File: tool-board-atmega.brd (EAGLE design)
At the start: 144 x 104 mm, 86 parts, among them IC3 ATMEGA2560-16AU, IC4 ATMEGA8U2-MU, Q1 16MHz, X1 22-23-2041, X2 MICROUSB_VERTICAL, X3 22-23-2041, X4 22-23-2041, Y2 16MHz

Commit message: significant routing done, need to beef up stepper related lines, add 24V stepper
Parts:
- moved U$2 191.4 mm to (-36.3, 44.8)
- moved U$3 191.4 mm to (-40.1, 44.8)
- moved U$4 191.4 mm to (-44.0, 44.8)
- moved U$5 191.4 mm to (-47.8, 44.8)
- moved F2 1.25 mm to (-19.6, 37.1)
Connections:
- new net N$38: F2.2, U$9.P$1
- net VCCPIN: no longer F2.2, U$9.P$1
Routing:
- net N$16: track 0.00 -> 148.2 mm, vias 0 -> 2
- net N$15: track 0.00 -> 129.1 mm, vias 0 -> 4
- net PB5: track 0.00 -> 115.4 mm, vias 0 -> 4
- net PB6: track 0.00 -> 114.3 mm, vias 0 -> 6
- net PB7: track 0.00 -> 104.5 mm, vias 0 -> 2
- net +12V: track 0.00 -> 97.8 mm
- net RESET: track 0.00 -> 97.3 mm, vias 0 -> 4
- net PA5: track 0.00 -> 95.5 mm, vias 0 -> 2
- net PA6: track 0.00 -> 92.6 mm, vias 0 -> 2
- net PA7: track 0.00 -> 77.5 mm, vias 0 -> 2
- net +5V: track 1.09 -> 72.0 mm, vias 1 -> 20
- net D-: track 0.00 -> 70.4 mm, vias 0 -> 1
- net PE0: track 0.00 -> 59.8 mm, vias 0 -> 2
- net PE1: track 0.00 -> 57.8 mm, vias 0 -> 4
- net D+: track 0.00 -> 53.4 mm, vias 0 -> 2
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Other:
- outline, holes or cut-outs redrawn

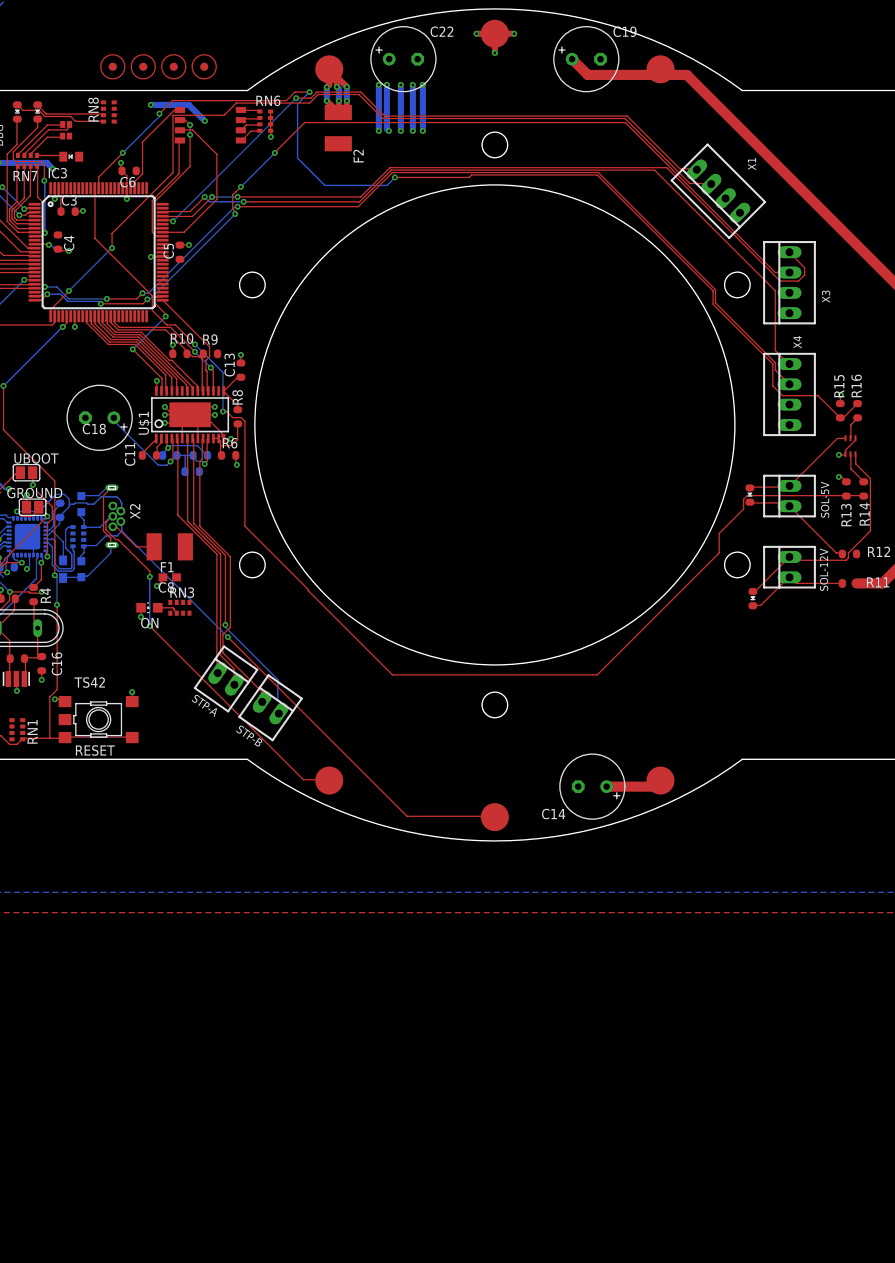
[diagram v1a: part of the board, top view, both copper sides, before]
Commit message: Beefed up 12V stepper lines, still need to work on 24V stepper lines.  Need to switch connectors for higher current ones
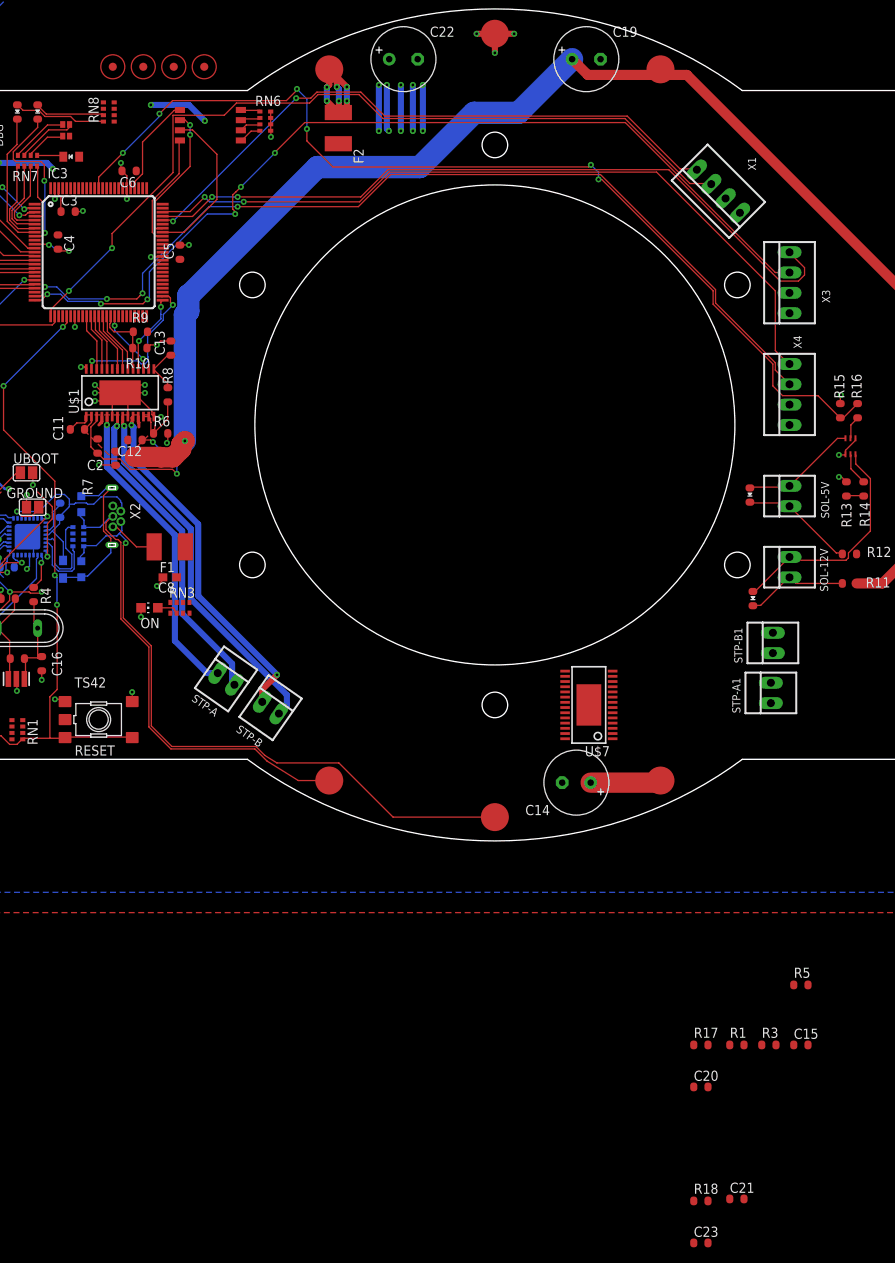
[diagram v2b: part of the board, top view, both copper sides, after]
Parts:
- removed C18: 100uF, rcl:E3,5-8
- added C15: .01u, SmartPrj:C0603-ROUND
- added C20: .47u, SmartPrj:C0603-ROUND
- added C21, C23: .1u, SmartPrj:C0603-ROUND
- added R1: 30k, SmartPrj:R0603-ROUND
- added R17, R5: 4.7k, SmartPrj:R0603-ROUND
- added R18: 1M, SmartPrj:R0603-ROUND
- added R3: 50k, SmartPrj:R0603-ROUND
- added STP-A1, STP-B1: 22-23-2021, con-molex:22-23-2021
- added U$7: DRV8825, ClinicalRobotics:DRV8825
- moved C2 9.71 mm to (-47.4, -4.15), flipped to the top, turned to 270 degrees
- moved C11 9.57 mm to (-52.2, -0.56)
- moved C13 9.17 mm to (-40.5, 9.60)
- moved R8 9.17 mm to (-40.9, 3.77)
- moved R9 9.17 mm to (-44.3, 11.6)
- moved U$1 9.17 mm to (-46.9, 4.02)
- moved R7 9.09 mm to (-49.7, -2.64), flipped to the top, turned to 90 degrees
- moved R6 8.93 mm to (-41.8, -1.06)
- moved C12 8.38 mm to (-45.0, -1.88), flipped to the top, turned to 180 degrees
- moved R10 5.06 mm to (-44.4, 9.61), turned to 0 degrees
- moved C14 2.06 mm to (10.2, -44.7)
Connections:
- removed net +12VIN: C12.2, C18.+, C2.1, R7.2, U$1.11, U$1.4
- removed net PC0: IC3.53
- removed net PC1: IC3.54
- removed net PC2: IC3.55
- removed net PC3: IC3.56
- removed net PC4: IC3.57
- removed net PC5: IC3.58
- removed net PC6: IC3.59
- removed net PC7: IC3.60
- new net DECAY-1: IC3.59, R17.1, R5.2, U$7.19
- new net DIR-1: IC3.58, U$7.20
- new net MODE0-1: IC3.55, U$7.24
- new net MODE1-1: IC3.54, U$7.25
- new net MODE2-1: IC3.53, U$7.26
- new net N$39: C15.1, U$7.1
- new net N$40: C15.2, U$7.2
- new net N$41: C20.1, R3.2, U$7.15
- new net N$42: R1.1, R3.1, U$7.12, U$7.13
- new net N$43: STP-A1.1, U$7.5
- new net N$44: STP-A1.2, U$7.7
- new net N$45: STP-B1.2, U$7.8
- new net N$46: STP-B1.1, U$7.10
- new net NENBL-1: IC3.57, U$7.21
- new net NFAULT-1: U$7.18
- new net NHOME-1: U$7.27
- new net NRESET-1: U$7.16
- new net NSLEEP-1: IC3.60, U$7.17
- new net NSTEP-1: IC3.56, U$7.22
- new net VCP-1: C21.1, R18.1, U$7.3
- net +12V: now also C12.2, C2.1, R7.2, U$1.11, U$1.4
- net +24V: now also C21.2, C23.1, R18.2, U$7.11, U$7.4
- net +5V: now also R5.1
- net GND: now also C20.2, C23.2, R1.2, R17.2, U$7.14, U$7.28, U$7.6, U$7.9, U$7.HEAT; no longer C18.-
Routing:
- net N$16: track 148.2 -> 2.19 mm, vias 2 -> 0
- net +12V: track 97.8 -> 186.8 mm, vias 0 -> 1
- net +12VIN: track 23.7 -> 0.00 mm, vias 2 -> 0
- net VCP: track 8.03 -> 23.1 mm, vias 1 -> 2
- net D-: track 70.4 -> 82.5 mm
- net NSLEEP: track 18.2 -> 8.14 mm
- net DECAY: track 19.5 -> 9.59 mm
- net DIR: track 16.2 -> 7.78 mm
- net MODE2: track 15.5 -> 7.17 mm
- net MODE0: track 15.6 -> 7.33 mm
- net MODE1: track 15.5 -> 7.29 mm
- net NENBL: track 15.9 -> 7.68 mm
- net NSTEP: track 15.9 -> 7.70 mm
- net D+: track 53.4 -> 60.6 mm, vias 2 -> 0
- net N$7: track 31.4 -> 38.6 mm, vias 0 -> 1
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- added copper zone on layer 1, net +12V

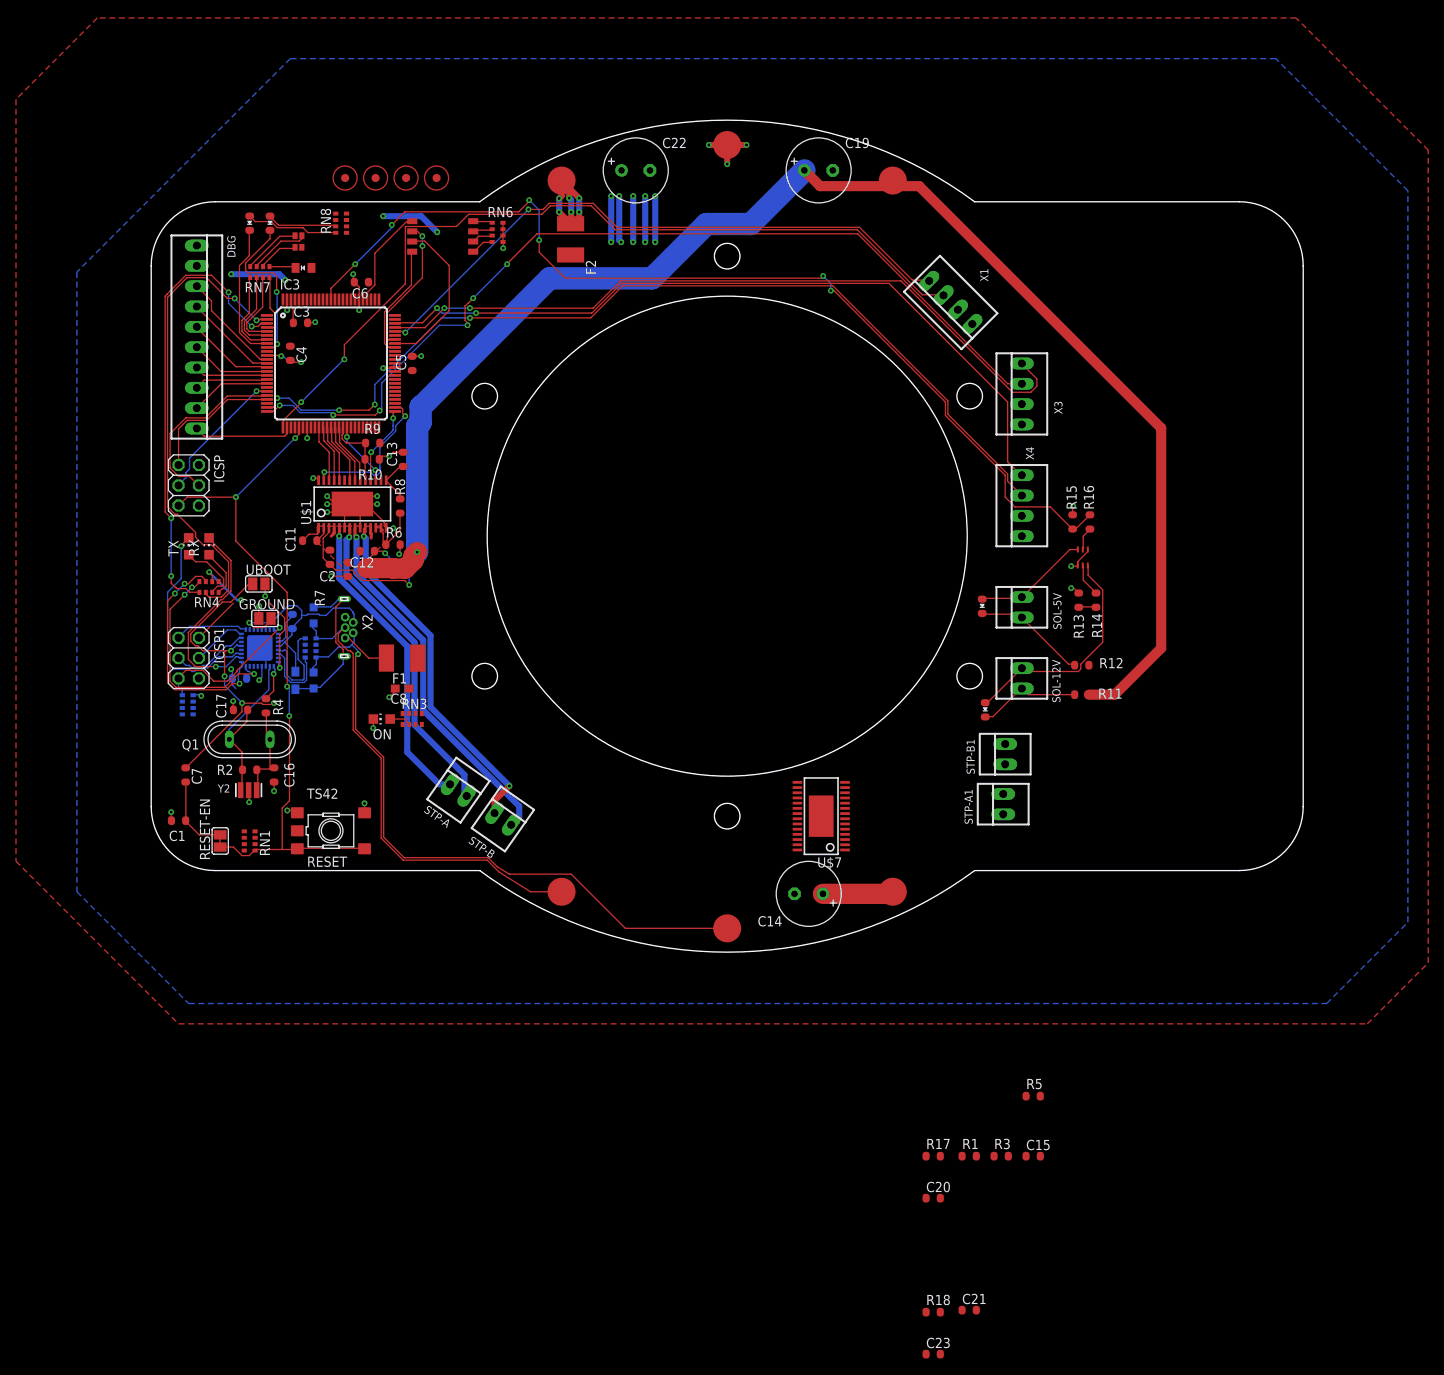
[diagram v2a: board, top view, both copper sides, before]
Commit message: Fixed stepper motor drivers for cleaner routing, moved them closer to power pogos
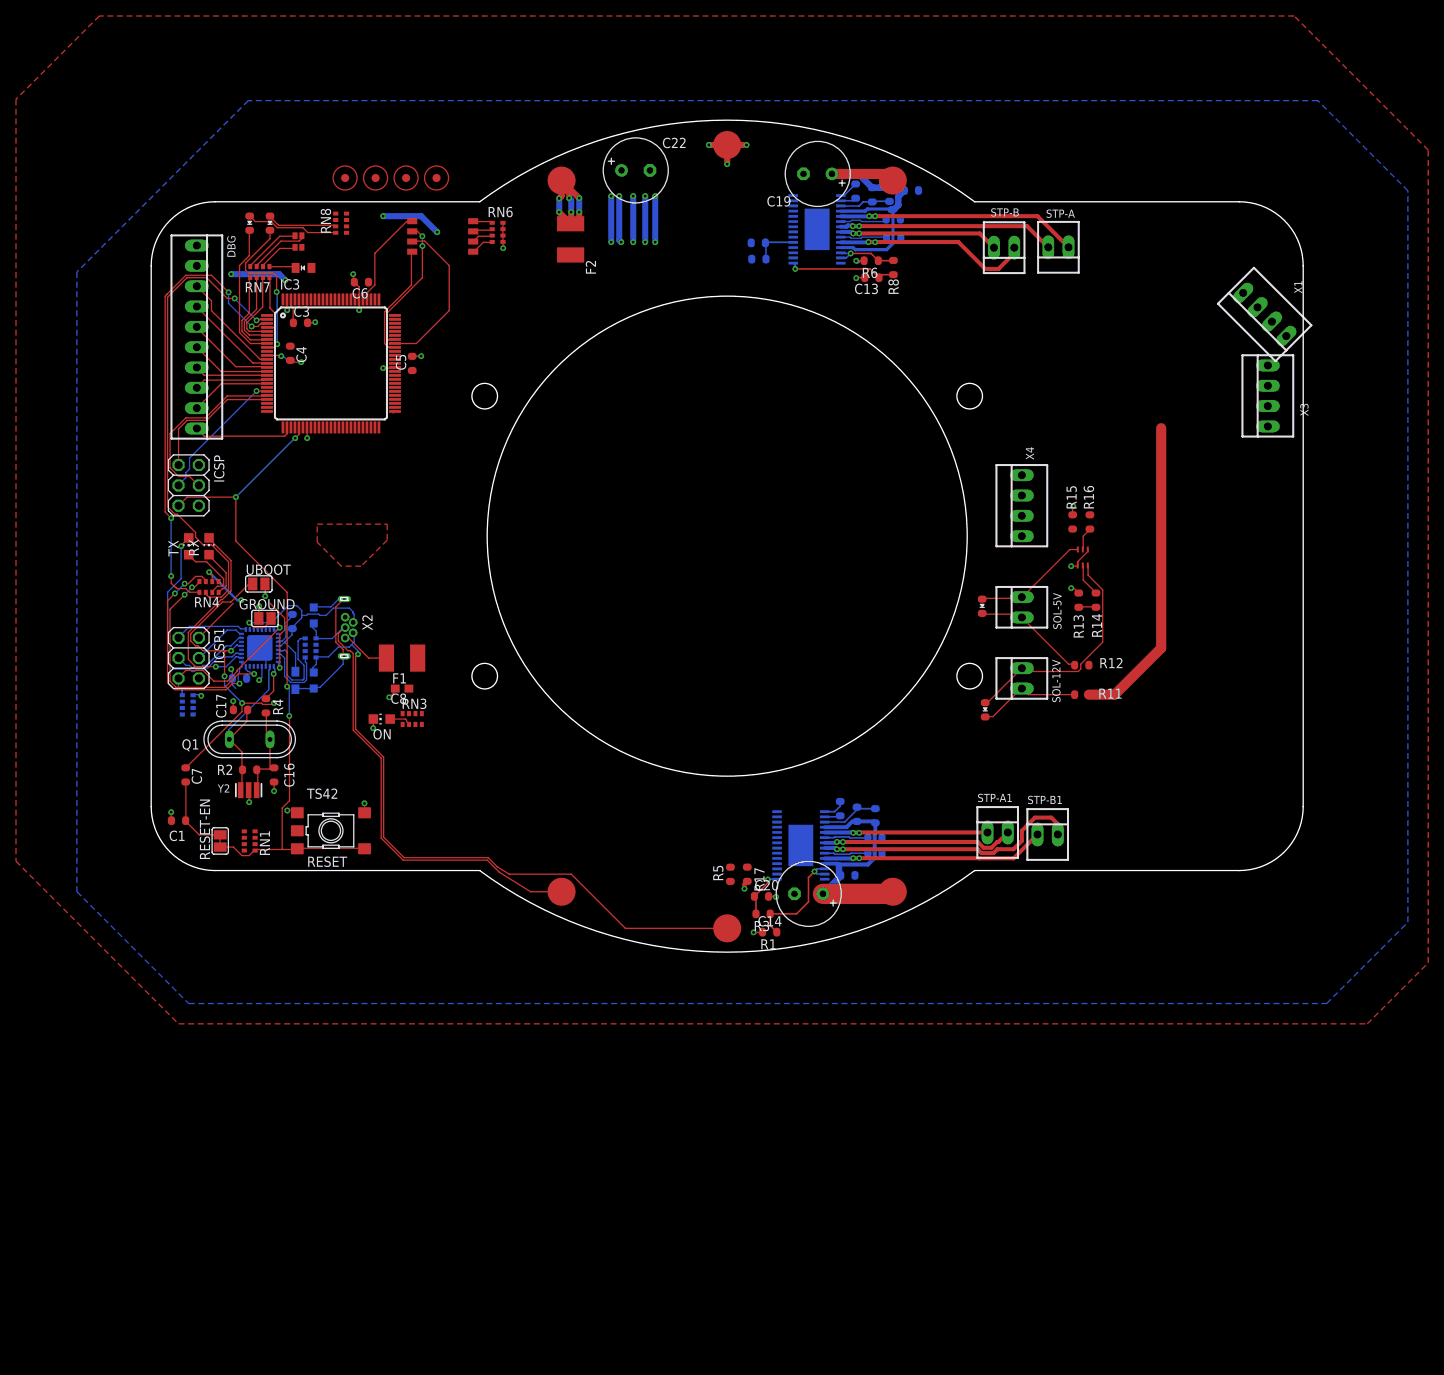
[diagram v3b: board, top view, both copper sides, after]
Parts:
- added R19, R20, R21, R22: 200m, SmartPrj:R0603-ROUND
- moved STP-A 101.1 mm to (41.4, 36.1), turned to 180 degrees
- moved STP-B 95.0 mm to (34.6, 36.1), turned to 180 degrees
- moved C2 84.9 mm to (23.0, 43.2), flipped to the bottom, turned to 180 degrees
- moved R7 83.4 mm to (20.3, 42.7), flipped to the bottom
- moved C11 81.0 mm to (16.1, 43.1), flipped to the bottom, turned to 270 degrees
- moved C12 77.3 mm to (18.1, 42.7), flipped to the bottom, turned to 90 degrees
- moved R6 69.5 mm to (18.0, 34.4), turned to 180 degrees
- moved R8 68.5 mm to (20.8, 33.6), turned to 270 degrees
- moved U$1 67.5 mm to (11.2, 38.4), flipped to the bottom, turned to 270 degrees
- moved R18 63.0 mm to (16.2, -34.8), flipped to the bottom, turned to 270 degrees
- moved C21 62.9 mm to (18.5, -34.9), flipped to the bottom, turned to 270 degrees
- moved C13 62.8 mm to (18.1, 32.3), turned to 180 degrees
- moved C23 60.8 mm to (15.1, -42.4), flipped to the bottom, turned to 180 degrees
- moved R10 54.4 mm to (3.96, 34.6), flipped to the bottom
- moved R9 54.3 mm to (3.89, 36.7), flipped to the bottom
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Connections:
- new net N$37: R19.2, U$7.9
- new net N$47: R20.2, U$7.6
- new net N$48: R21.2, U$1.6
- new net N$49: R22.2, U$1.9
- net DECAY: now also IC3.54; no longer IC3.41
- net DECAY-1: now also IC3.36; no longer IC3.59
- net DIR: now also IC3.55; no longer IC3.40
- net DIR-1: now also IC3.37; no longer IC3.58
- net GND: now also R19.1, R20.1, R21.1, R22.1; no longer U$1.6, U$1.9, U$7.6, U$7.9
- net MODE0: now also IC3.58; no longer IC3.37
- net MODE0-1: now also IC3.40; no longer IC3.55
- net MODE1: now also IC3.59; no longer IC3.36
- net MODE1-1: now also IC3.41; no longer IC3.54
- net MODE2: now also IC3.60; no longer IC3.35
- net MODE2-1: now also IC3.42; no longer IC3.53
- net NENBL: now also IC3.56; no longer IC3.39
- net NENBL-1: now also IC3.38; no longer IC3.57
- net NFAULT-1: now also IC3.70
- net NHOME-1: now also IC3.28
- net NSLEEP: now also IC3.53; no longer IC3.42
- net NSLEEP-1: now also IC3.35; no longer IC3.60
- net NSTEP: now also IC3.57; no longer IC3.38
- net NSTEP-1: now also IC3.39; no longer IC3.56
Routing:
- net N$15: track 125.2 -> 0.00 mm, vias 6 -> 0
- net PB5: track 116.6 -> 0.00 mm, vias 4 -> 0
- net PB6: track 116.2 -> 0.00 mm, vias 6 -> 0
- net +12V: track 186.8 -> 78.7 mm, vias 1 -> 0
- net PB7: track 104.5 -> 0.00 mm, vias 2 -> 0
- net PA5: track 95.2 -> 0.00 mm, vias 2 -> 0
- net PA6: track 92.4 -> 0.00 mm, vias 2 -> 0
- net PA7: track 77.5 -> 0.00 mm, vias 2 -> 0
- net N$45: track 0.00 -> 34.4 mm, vias 0 -> 2
- net GND: track 81.4 -> 52.6 mm, vias 36 -> 31
- net N$46: track 0.00 -> 28.6 mm, vias 0 -> 2
- net N$12: track 46.0 -> 20.7 mm, vias 1 -> 2
- net N$44: track 0.00 -> 24.8 mm, vias 0 -> 2
- net +24V: track 8.84 -> 31.7 mm
- net N$43: track 0.00 -> 21.2 mm, vias 0 -> 2
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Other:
- outline, holes or cut-outs redrawn

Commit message: board Rev01 done, needs review by Jaden and to clean up labels
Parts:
- removed U$2, U$3, U$4, U$5: FIDUCIALMOUNT, SmartPrj:FIDUCIA-MOUNT
- added A: 22-23-2081, con-molex:22-23-2081
- added SV1, SV2, SV3: (no value), con-lstb:MA03-1
- added X5, X6: (no value), con-phoenix-254:12POL254
- added X7: (no value), con-phoenix-254:4POL254
- moved X3 25.5 mm to (42.2, 15.0)
- moved X1 25.1 mm to (42.1, 27.8), turned to 90 degrees
- moved STP-B 7.62 mm to (27.0, 36.1)
- moved STP-A 6.35 mm to (35.1, 36.1)
- moved C5 5.75 mm to (-45.1, 21.0), flipped to the bottom
- moved C3 2.18 mm to (-55.1, 25.4), flipped to the bottom, turned to 270 degrees
- moved F2 2.05 mm to (-20.6, 38.9)
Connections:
- new net N$50: A.1, IC3.90
- new net N$51: A.2, IC3.91
- new net N$52: A.3, IC3.92
- new net N$53: A.4, IC3.93
- new net N$56: A.5, IC3.94
- new net N$57: A.6, IC3.95
- new net N$58: A.7, IC3.96
- new net N$59: A.8, IC3.97
- new net N$60: SV1.2, X4.2
- new net N$61: SV2.2, X3.2
- new net N$62: SV3.2, X1.2
- net +12V: now also SV1.1, SV2.1, SV3.1, X6.10, X6.11, X6.12, X6.7, X6.8, X6.9
- net +24V: now also X7.1, X7.2, X7.3, X7.4
- net +5V: now also SV1.3, SV2.3, SV3.3, X6.1, X6.2, X6.3, X6.4, X6.5, X6.6; no longer X1.2, X3.2, X4.2
- net GND: now also X5.1, X5.10, X5.11, X5.12, X5.2, X5.3, X5.4, X5.5, X5.6, X5.7, X5.8, X5.9
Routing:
- net N$15: track 0.00 -> 190.5 mm, vias 0 -> 8
- net N$16: track 2.19 -> 169.8 mm, vias 0 -> 8
- net PB6: track 0.00 -> 129.6 mm, vias 0 -> 4
- net PB5: track 0.00 -> 127.5 mm, vias 0 -> 5
- net PB7: track 0.00 -> 122.8 mm, vias 0 -> 6
- net NHOME: track 0.12 -> 116.1 mm, vias 0 -> 1
- net NFAULT-1: track 0.00 -> 107.8 mm, vias 0 -> 5
- net PA6: track 0.00 -> 98.8 mm, vias 0 -> 4
- net PA5: track 0.00 -> 97.2 mm, vias 0 -> 3
- net NSLEEP-1: track 0.00 -> 97.0 mm, vias 0 -> 1
- net DECAY-1: track 0.00 -> 96.7 mm, vias 0 -> 3
- net PA7: track 0.00 -> 95.2 mm, vias 0 -> 2
- net DIR-1: track 0.00 -> 94.5 mm, vias 0 -> 1
- net NENBL-1: track 0.00 -> 93.4 mm, vias 0 -> 1
- net NSTEP-1: track 0.00 -> 92.5 mm, vias 0 -> 1
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- removed copper zone on layer 1, net +12V
